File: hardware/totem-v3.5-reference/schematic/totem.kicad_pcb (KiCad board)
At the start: 4 copper layers, 45.8 x 46.4 mm, 136 parts, among them J1 USB4135-GF-A, J2 LiPo 1000mAh, J3 u.FL, Q1 AO3401A, Q2 2N7002, Q3 2N7002, Q4 AO3401A, Q5 2N7002, SW1 power, SW2 SOS, U1 ESP32-WROOM-32E, U2 MAX-M10S, U3 TP4056-42-ESOP8, U4 AP2112K-3.3, U5 ICM-20948

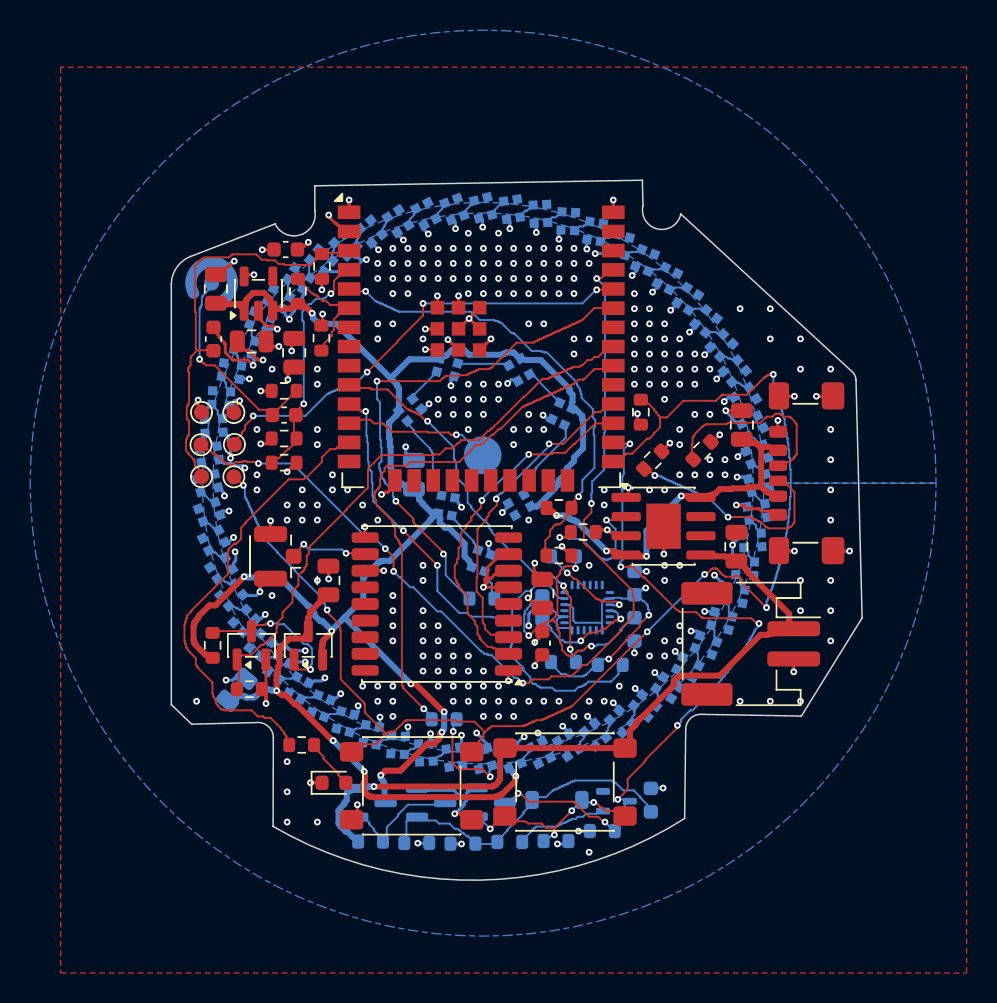
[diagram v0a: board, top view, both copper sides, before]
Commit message: fix: a 50-ohm GNSS feed, and margins that hold at the board edge
The u.FL to MAX-M10S feed was an ordinary 0.13 mm track (~80 ohms over
In1). It is now its own net class, 0.38 mm with 0.3 mm to other copper
(50 ohms on a 1.6 mm 4-layer stack-up, ~0.21 mm of 7628 over In1), kept
on F.Cu and via-free: a straight 4.8 mm microstrip. C15 moves to clear
its path.

The router keeps 0.07 mm extra from the rasterised outline (arcs lost a
few um), and the inner GND pour's minimum width is 0.25 mm so it has no
necks under the minimum connection; the VLED pour keeps 0.2 mm, which it
needs beside the tab notch.

DRC with schematic parity, all severities: 0 / 0 / 0.

Claude-Session: https://claude.ai/code/session_0192KwQN6XkBBxwoQn8x3FMV
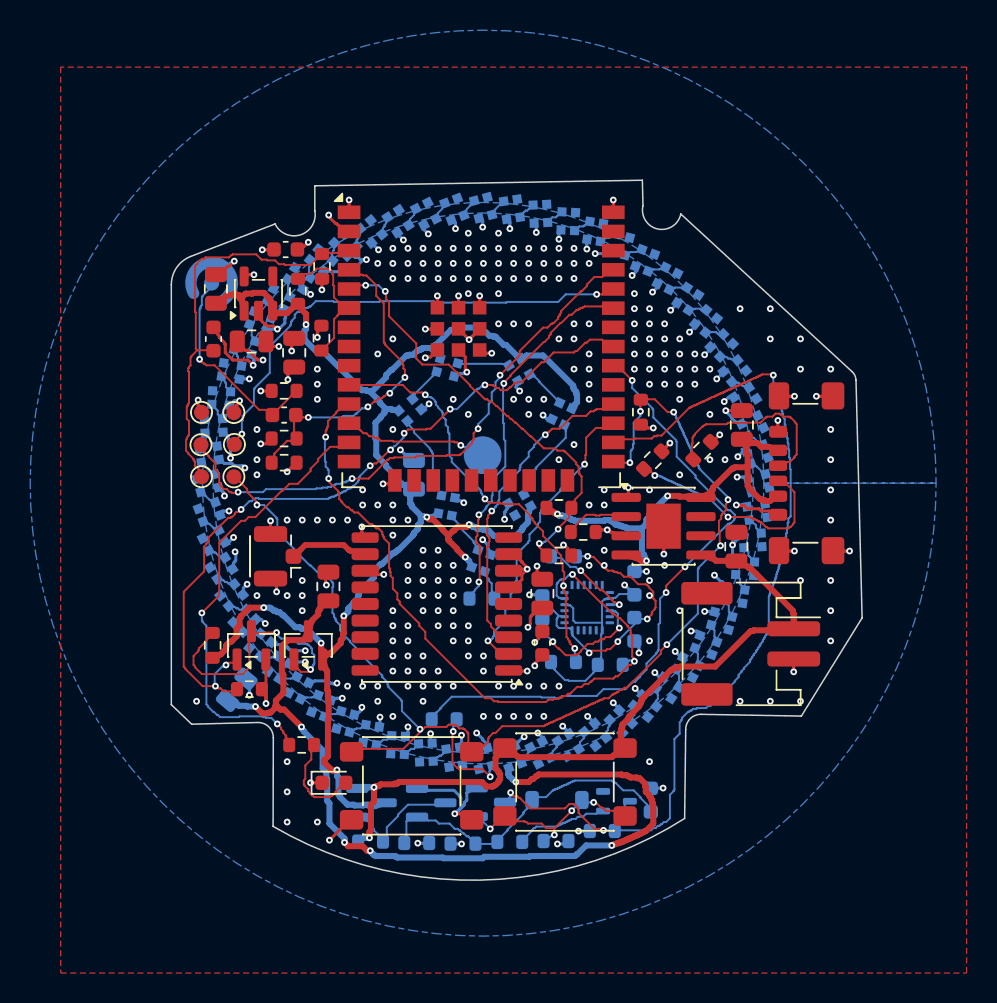
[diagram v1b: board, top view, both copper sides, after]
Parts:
- moved C15 0.40 mm to (87.7, 104.4)
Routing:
- net /TXD0: track 63.7 -> 37.5 mm, vias 6 -> 4
- net VLED: track 33.1 -> 58.8 mm, vias 4 -> 6
- net /GPIO4: track 47.6 -> 61.8 mm, vias 7 -> 3
- net /BTN_SOS: track 89.0 -> 75.3 mm, vias 6 -> 8
- net /LED_EN: track 38.3 -> 49.2 mm, vias 0 -> 8
- net /CRYSTAL_DATA: track 34.7 -> 25.1 mm
- net /I2C0_SCL: track 38.1 -> 47.4 mm, vias 3 -> 4
- net /RING_GATE: track 10.5 -> 17.0 mm
- net /MIC: track 15.6 -> 21.5 mm, vias 2 -> 4
- net /RING_DATA: track 36.3 -> 42.0 mm, vias 1 -> 3
- net +3V3: track 40.4 -> 35.1 mm, vias 19 -> 17
- net /PROG: track 9.19 -> 4.24 mm, vias 2 -> 0
- net GND: track 153.9 -> 150.0 mm, vias 338 -> 329
- net /GNSS_TX: track 23.7 -> 20.0 mm
- net VSYS: track 101.4 -> 97.9 mm, vias 7 -> 8
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
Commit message: fix: power vias that carry their current, and QA that does not trust KiCad alone
- VBAT/VSYS/VBUS/VLED vias are 0.6/0.3 mm: a 0.2 mm barrel had about the
  copper of the 0.4 mm track feeding it, on paths that carry ~1 A
- the LED budget deck uses the 1515's datasheet current (15.5 mA at full
  white): all 67 pixels at the firmware's brightness are 0.62 C, a check
  now, not a known limit; the empty cell is the firmware's 3.15 V. Block
  sims 18/0/1, board sim 78/0/1
- gerber_check.py reads the gerbers back with gerbonara: all ten graphic
  layers present, outline 45.753 x 46.361 mm against the measured 45.753 x
  46.360, drills 382 x 0.2 and 12 x 0.3 mm
- the ring's 59 LED-to-LED links are all 1.18-1.25 mm: every LED faces
  the right way
- DRC with --refill-zones and schematic parity: 0 / 0 / 0

Claude-Session: https://claude.ai/code/session_0192KwQN6XkBBxwoQn8x3FMV
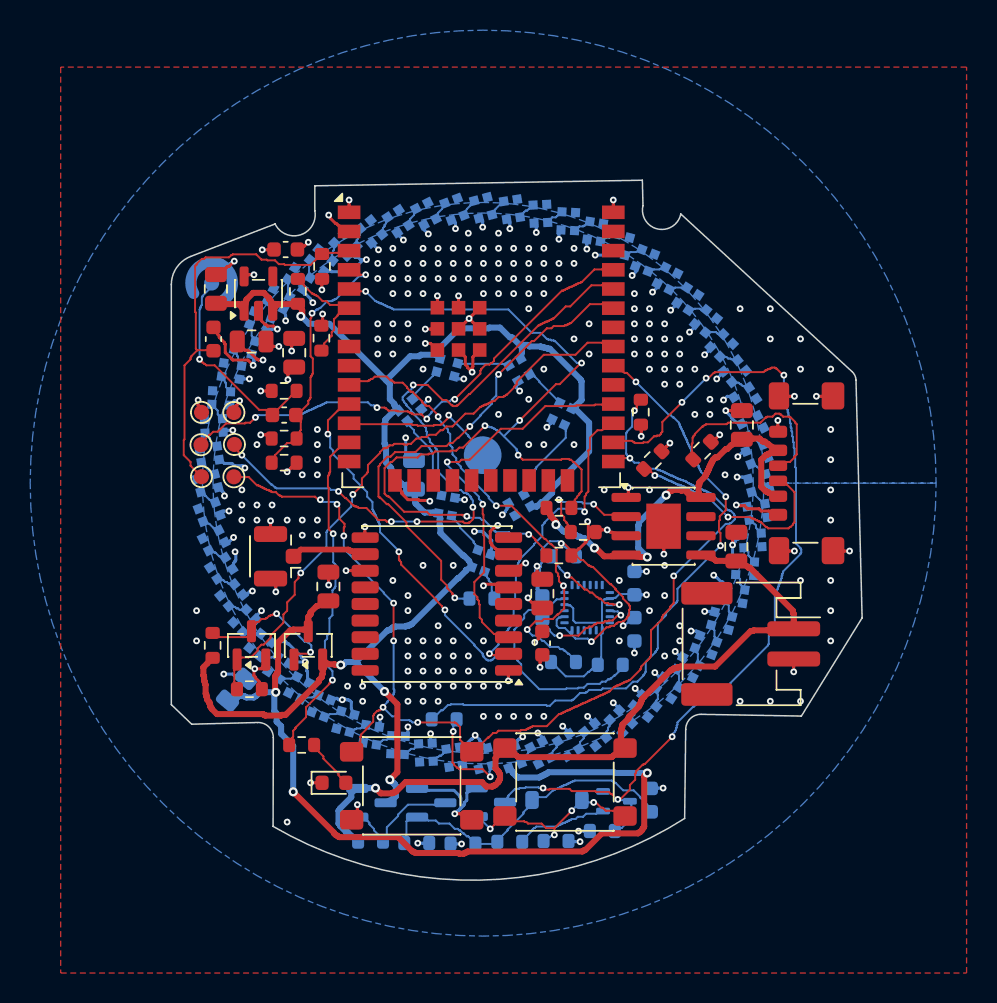
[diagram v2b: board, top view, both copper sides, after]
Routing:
- net /VBUS_SENSE: track 29.1 -> 57.2 mm, vias 4 -> 7
- net /RXD0: track 32.1 -> 46.8 mm, vias 2 -> 6
- net /LED_EN: track 49.2 -> 38.8 mm, vias 8 -> 2
- net /I2C0_SCL: track 47.4 -> 39.4 mm, vias 4 -> 3
- net /CRYSTAL_DATA: track 25.1 -> 32.9 mm
- net /SOS_LED: track 29.7 -> 22.6 mm
- net /RING_GATE: track 17.0 -> 10.1 mm
- net GND: track 150.0 -> 156.3 mm, vias 329 -> 289
- net /GNSS_RX: track 21.2 -> 26.8 mm
- net /MIC: track 21.5 -> 17.2 mm, vias 4 -> 2
- net /TXD0: track 37.5 -> 33.4 mm
- net /SOS_LED_A: track 6.51 -> 3.34 mm
- net /PROG: track 4.24 -> 7.30 mm, vias 0 -> 2
- net /I2C0_SDA: track 29.0 -> 31.8 mm
- net /REGOUT: track 8.96 -> 7.20 mm
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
